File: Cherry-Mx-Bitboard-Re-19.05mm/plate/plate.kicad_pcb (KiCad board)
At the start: 2 copper layers, 106 x 106 mm, 396 parts, among them SW1 SW_Push

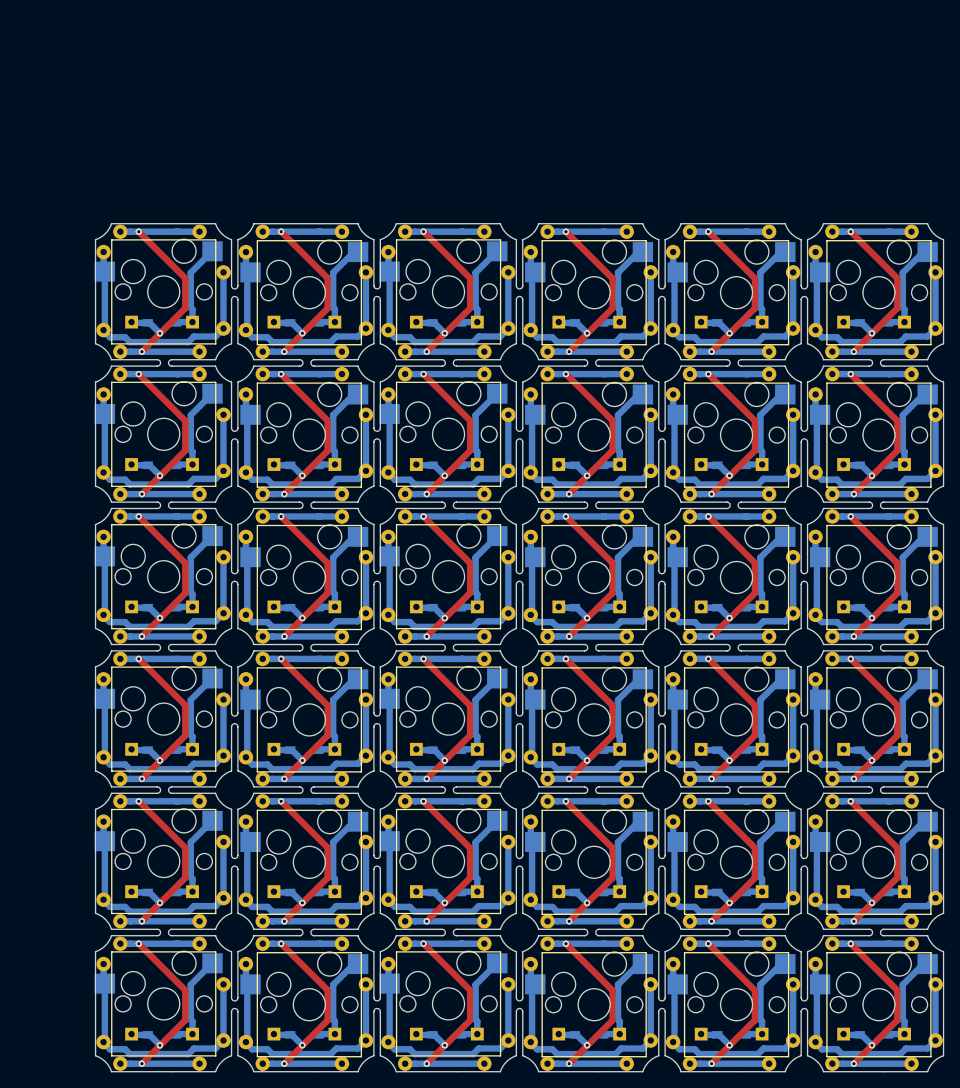
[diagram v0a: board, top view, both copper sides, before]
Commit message: Plate generaged with gerber
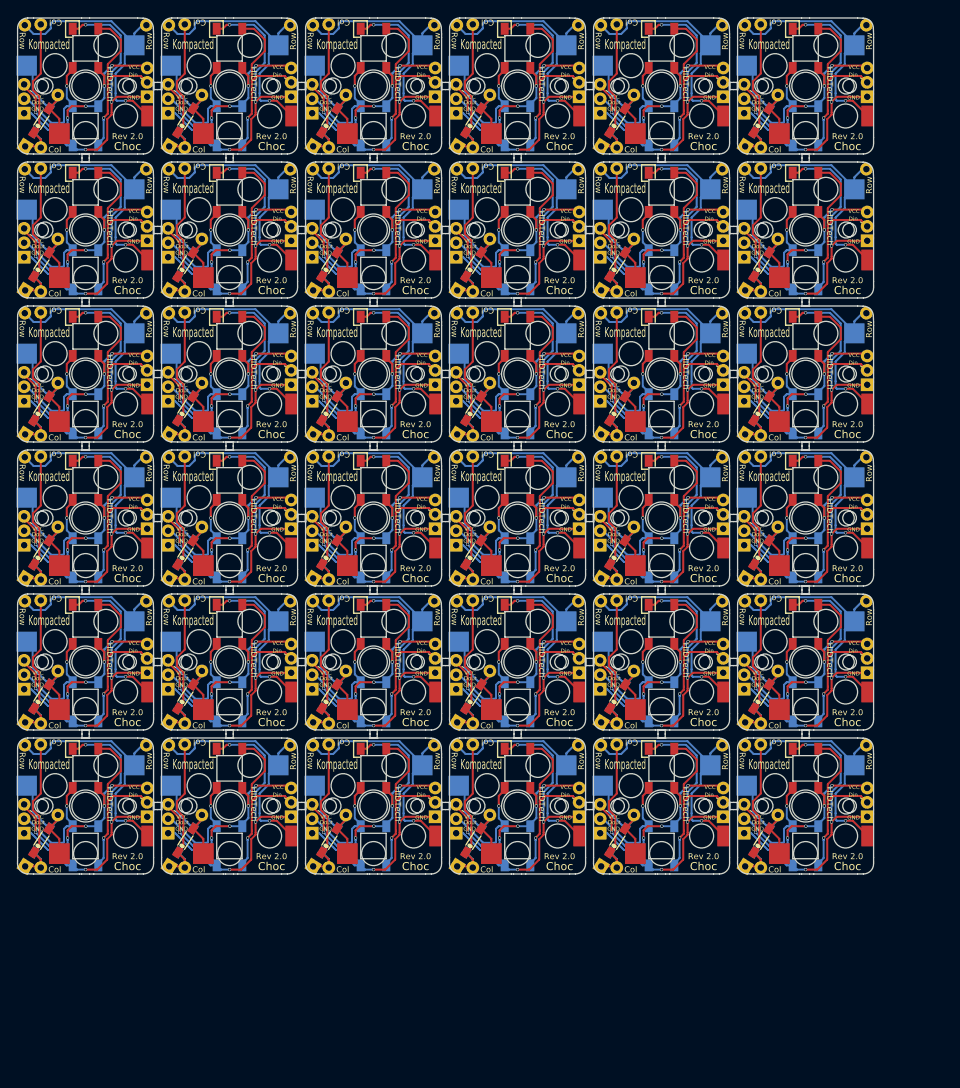
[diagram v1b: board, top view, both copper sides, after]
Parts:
- removed Col111 (x36), Col114 (x36), Row112 (x36), Row114 (x36): Conn_01x01, Footprints:Wirepad
- removed the Col112 at (178.1, 161.0)
- removed the Col112 at (124.7, 143.2)
- removed the Col112 at (142.5, 143.2)
- removed the Col112 at (106.9, 143.2)
- removed the Col112 at (178.1, 125.4)
- removed the Col112 at (195.9, 125.4)
- removed the Col112 at (160.3, 125.4)
- removed the Col112 at (124.7, 125.4)
- removed the Col112 at (142.5, 125.4)
- removed the Col112 at (106.9, 125.4)
- removed the Col112 at (178.1, 107.6)
- removed the Col112 at (195.9, 161.0)
- removed the Col112 at (195.9, 107.6)
- removed the Col112 at (160.3, 107.6)
- removed the Col112 at (124.7, 107.6)
- removed the Col112 at (142.5, 107.6)
- removed the Col112 at (106.9, 107.6)
- removed the Col112 at (195.9, 89.8)
- removed the Col112 at (178.1, 89.8)
- removed the Col112 at (124.7, 89.8)
- removed the Col112 at (160.3, 89.8)
- removed the Col112 at (142.5, 89.8)
- removed the Col112 at (160.3, 161.0)
- removed the Col112 at (106.9, 89.8)
- removed the Col112 at (195.9, 72.0)
- removed the Col112 at (178.1, 72.0)
- removed the Col112 at (160.3, 72.0)
- removed the Col112 at (142.5, 72.0)
- removed the Col112 at (124.7, 72.0)
- removed the Col112 at (106.9, 72.0)
- removed the Col112 at (124.7, 161.0)
- removed the Col112 at (142.5, 161.0)
- removed the Col112 at (106.9, 161.0)
- removed the Col112 at (178.1, 143.2)
- removed the Col112 at (195.9, 143.2)
- removed the Col112 at (160.3, 143.2)
- removed the Col113 at (186.0, 176.0)
- removed the Col113 at (114.8, 158.2)
- removed the Col113 at (168.2, 158.2)
- removed the Col113 at (97.0, 158.2)
- removed the Col113 at (186.0, 140.4)
- removed the Col113 at (150.4, 140.4)
- removed the Col113 at (132.6, 140.4)
- removed the Col113 at (114.8, 140.4)
- removed the Col113 at (168.2, 140.4)
- removed the Col113 at (97.0, 140.4)
- removed the Col113 at (186.0, 122.6)
- removed the Col113 at (150.4, 176.0)
- removed the Col113 at (150.4, 122.6)
- removed the Col113 at (132.6, 122.6)
- removed the Col113 at (114.8, 122.6)
- removed the Col113 at (168.2, 122.6)
- removed the Col113 at (97.0, 122.6)
- removed the Col113 at (186.0, 104.8)
- removed the Col113 at (168.2, 104.8)
- removed the Col113 at (114.8, 104.8)
- removed the Col113 at (132.6, 104.8)
- removed the Col113 at (150.4, 104.8)
- removed the Col113 at (132.6, 176.0)
- removed the Col113 at (97.0, 104.8)
- removed the Col113 at (186.0, 87.0)
- removed the Col113 at (168.2, 87.0)
- removed the Col113 at (150.4, 87.0)
- removed the Col113 at (132.6, 87.0)
- removed the Col113 at (114.8, 87.0)
- removed the Col113 at (97.0, 87.0)
- removed the Col113 at (114.8, 176.0)
- removed the Col113 at (168.2, 176.0)
- removed the Col113 at (97.0, 176.0)
- removed the Col113 at (186.0, 158.2)
- removed the Col113 at (150.4, 158.2)
- removed the Col113 at (132.6, 158.2)
- removed the D1 at (169.6, 172.3)
- removed the D1 at (134.0, 154.5)
- removed the D1 at (151.8, 154.5)
- removed the D1 at (98.4, 154.5)
- removed the D1 at (169.6, 136.7)
- removed the D1 at (187.4, 136.7)
- removed the D1 at (116.2, 136.7)
- removed the D1 at (134.0, 136.7)
- removed the D1 at (151.8, 136.7)
- removed the D1 at (98.4, 136.7)
- removed the D1 at (169.6, 118.9)
- removed the D1 at (187.4, 172.3)
- removed the D1 at (187.4, 118.9)
- removed the D1 at (116.2, 118.9)
- removed the D1 at (134.0, 118.9)
- removed the D1 at (151.8, 118.9)
- removed the D1 at (98.4, 118.9)
- removed the D1 at (187.4, 101.1)
- removed the D1 at (169.6, 101.1)
- removed the D1 at (116.2, 101.1)
- removed the D1 at (134.0, 101.1)
- removed the D1 at (151.8, 101.1)
- removed the D1 at (116.2, 172.3)
- removed the D1 at (98.4, 101.1)
- removed the D1 at (187.4, 83.3)
- removed the D1 at (169.6, 83.3)
- removed the D1 at (151.8, 83.3)
- removed the D1 at (134.0, 83.3)
- removed the D1 at (116.2, 83.3)
- removed the D1 at (98.4, 83.3)
- removed the D1 at (134.0, 172.3)
- removed the D1 at (151.8, 172.3)
- removed the D1 at (98.4, 172.3)
- removed the D1 at (169.6, 154.5)
- removed the D1 at (187.4, 154.5)
- removed the D1 at (116.2, 154.5)
- removed the D2 at (191.2, 172.4)
- removed the D2 at (155.6, 154.6)
- removed the D2 at (137.8, 154.6)
- removed the D2 at (102.2, 154.6)
- removed the D2 at (191.2, 136.8)
- removed the D2 at (120.0, 136.8)
- removed the D2 at (173.4, 136.8)
- removed the D2 at (155.6, 136.8)
- removed the D2 at (137.8, 136.8)
- removed the D2 at (102.2, 136.8)
- removed the D2 at (191.2, 119.0)
- removed the D2 at (120.0, 172.4)
- removed the D2 at (120.0, 119.0)
- removed the D2 at (173.4, 119.0)
- removed the D2 at (155.6, 119.0)
- removed the D2 at (137.8, 119.0)
- removed the D2 at (102.2, 119.0)
- removed the D2 at (191.2, 101.2)
- removed the D2 at (173.4, 101.2)
- removed the D2 at (120.0, 101.2)
- removed the D2 at (137.8, 101.2)
- removed the D2 at (155.6, 101.2)
- removed the D2 at (173.4, 172.4)
- removed the D2 at (102.2, 101.2)
- removed the D2 at (191.2, 83.4)
- removed the D2 at (173.4, 83.4)
- removed the D2 at (155.6, 83.4)
- removed the D2 at (137.8, 83.4)
- removed the D2 at (120.0, 83.4)
- removed the D2 at (102.2, 83.4)
- removed the D2 at (155.6, 172.4)
- removed the D2 at (137.8, 172.4)
- removed the D2 at (102.2, 172.4)
- removed the D2 at (191.2, 154.6)
- removed the D2 at (120.0, 154.6)
- removed the D2 at (173.4, 154.6)
- removed the Row111 at (183.9, 163.6)
- removed the Row111 at (112.7, 145.8)
- removed the Row111 at (94.9, 145.8)
- removed the Row111 at (148.3, 145.8)
- removed the Row111 at (183.9, 128.0)
- removed the Row111 at (166.1, 128.0)
- removed the Row111 at (130.5, 128.0)
- removed the Row111 at (112.7, 128.0)
- removed the Row111 at (94.9, 128.0)
- removed the Row111 at (148.3, 128.0)
- removed the Row111 at (183.9, 110.2)
- removed the Row111 at (166.1, 163.6)
- removed the Row111 at (166.1, 110.2)
- removed the Row111 at (130.5, 110.2)
- removed the Row111 at (112.7, 110.2)
- removed the Row111 at (94.9, 110.2)
- removed the Row111 at (148.3, 110.2)
- removed the Row111 at (183.9, 92.4)
- removed the Row111 at (166.1, 92.4)
- removed the Row111 at (112.7, 92.4)
- removed the Row111 at (130.5, 92.4)
- removed the Row111 at (148.3, 92.4)
- removed the Row111 at (130.5, 163.6)
- removed the Row111 at (94.9, 92.4)
- removed the Row111 at (183.9, 74.6)
- removed the Row111 at (166.1, 74.6)
- removed the Row111 at (148.3, 74.6)
- removed the Row111 at (130.5, 74.6)
- removed the Row111 at (112.7, 74.6)
- removed the Row111 at (112.7, 163.6)
- removed the Row111 at (94.9, 163.6)
- removed the Row111 at (148.3, 163.6)
- removed the Row111 at (183.9, 145.8)
- removed the Row111 at (166.1, 145.8)
- removed the Row111 at (130.5, 145.8)
- removed the Row113 at (181.1, 166.1)
- removed the Row113 at (163.3, 148.3)
- removed the Row113 at (127.7, 148.3)
- removed the Row113 at (145.5, 148.3)
- removed the Row113 at (181.1, 130.5)
- removed the Row113 at (198.9, 130.5)
- removed the Row113 at (109.9, 130.5)
- removed the Row113 at (163.3, 130.5)
- removed the Row113 at (127.7, 130.5)
- removed the Row113 at (145.5, 130.5)
- removed the Row113 at (181.1, 112.7)
- removed the Row113 at (198.9, 166.1)
- removed the Row113 at (198.9, 112.7)
- removed the Row113 at (109.9, 112.7)
- removed the Row113 at (163.3, 112.7)
- removed the Row113 at (127.7, 112.7)
- removed the Row113 at (145.5, 112.7)
- removed the Row113 at (198.9, 94.9)
- removed the Row113 at (181.1, 94.9)
- removed the Row113 at (109.9, 94.9)
- removed the Row113 at (127.7, 94.9)
- removed the Row113 at (163.3, 94.9)
- removed the Row113 at (109.9, 166.1)
- removed the Row113 at (145.5, 94.9)
- removed the Row113 at (198.9, 77.1)
- removed the Row113 at (181.1, 77.1)
- removed the Row113 at (145.5, 77.1)
- removed the Row113 at (163.3, 77.1)
- removed the Row113 at (127.7, 77.1)
- removed the Row113 at (163.3, 166.1)
- removed the Row113 at (127.7, 166.1)
- removed the Row113 at (145.5, 166.1)
- removed the Row113 at (181.1, 148.3)
- removed the Row113 at (198.9, 148.3)
- removed the Row113 at (109.9, 148.3)
- removed the SW1 at (191.8, 168.7)
- removed the SW1 at (138.0, 150.8)
- removed the SW1 at (156.2, 150.9)
- removed the SW1 at (102.4, 150.8)
- removed the SW1 at (191.8, 133.1)
- removed the SW1 at (174.0, 133.1)
- removed the SW1 at (120.6, 133.1)
- removed the SW1 at (138.0, 133.0)
- removed the SW1 at (156.2, 133.1)
- removed the SW1 at (102.4, 133.0)
- removed the SW1 at (191.8, 115.3)
- removed the SW1 at (174.0, 168.7)
- removed the SW1 at (174.0, 115.3)
- removed the SW1 at (120.6, 115.3)
- removed the SW1 at (138.0, 115.2)
- removed the SW1 at (156.2, 115.3)
- removed the SW1 at (102.4, 115.2)
- removed the SW1 at (191.8, 97.5)
- removed the SW1 at (174.0, 97.5)
- removed the SW1 at (120.6, 97.5)
- removed the SW1 at (156.2, 97.5)
- removed the SW1 at (138.0, 97.4)
- removed the SW1 at (120.6, 168.7)
- removed the SW1 at (102.4, 97.4)
- removed the SW1 at (191.8, 79.7)
- removed the SW1 at (174.0, 79.7)
- removed the SW1 at (156.2, 79.7)
- removed the SW1 at (138.0, 79.6)
- removed the SW1 at (120.6, 79.7)
- removed the SW1 at (102.4, 79.6)
- removed the SW1 at (138.0, 168.6)
- removed the SW1 at (156.2, 168.7)
- removed the SW1 at (102.4, 168.6)
- removed the SW1 at (191.8, 150.9)
- removed the SW1 at (174.0, 150.9)
- removed the SW1 at (120.6, 150.9)
- added Col112: Conn_01x01, Footprints:Wirepad, F.Cu at (87.0, 118.1)
- added Col112: Conn_01x01, Footprints:Wirepad, F.Cu at (177.0, 118.1)
- added Col112: Conn_01x01, Footprints:Wirepad, F.Cu at (141.0, 118.1)
- added Col112: Conn_01x01, Footprints:Wirepad, F.Cu at (123.0, 118.1)
- added Col112: Conn_01x01, Footprints:Wirepad, F.Cu at (87.0, 82.1)
- added Col112: Conn_01x01, Footprints:Wirepad, F.Cu at (105.0, 82.1)
- added Col112: Conn_01x01, Footprints:Wirepad, F.Cu at (87.0, 100.1)
- added Col112: Conn_01x01, Footprints:Wirepad, F.Cu at (105.0, 100.1)
- added Col112: Conn_01x01, Footprints:Wirepad, F.Cu at (159.0, 100.1)
- added Col112: Conn_01x01, Footprints:Wirepad, F.Cu at (177.0, 100.1)
- added Col112: Conn_01x01, Footprints:Wirepad, F.Cu at (123.0, 100.1)
- added Col112: Conn_01x01, Footprints:Wirepad, F.Cu at (105.0, 118.1)
- added Col112: Conn_01x01, Footprints:Wirepad, F.Cu at (141.0, 100.1)
- added Col112: Conn_01x01, Footprints:Wirepad, F.Cu at (159.0, 82.1)
- added Col112: Conn_01x01, Footprints:Wirepad, F.Cu at (177.0, 82.1)
- added Col112: Conn_01x01, Footprints:Wirepad, F.Cu at (141.0, 82.1)
- added Col112: Conn_01x01, Footprints:Wirepad, F.Cu at (123.0, 82.1)
- added Col112: Conn_01x01, Footprints:Wirepad, F.Cu at (87.0, 64.1)
- added Col112: Conn_01x01, Footprints:Wirepad, F.Cu at (105.0, 64.1)
- added Col112: Conn_01x01, Footprints:Wirepad, F.Cu at (159.0, 64.1)
- added Col112: Conn_01x01, Footprints:Wirepad, F.Cu at (177.0, 64.1)
- added Col112: Conn_01x01, Footprints:Wirepad, F.Cu at (141.0, 64.1)
- added Col112: Conn_01x01, Footprints:Wirepad, F.Cu at (87.0, 136.1)
- added Col112: Conn_01x01, Footprints:Wirepad, F.Cu at (123.0, 64.1)
- added Col112: Conn_01x01, Footprints:Wirepad, F.Cu at (159.0, 46.1)
- added Col112: Conn_01x01, Footprints:Wirepad, F.Cu at (177.0, 46.1)
- added Col112: Conn_01x01, Footprints:Wirepad, F.Cu at (123.0, 46.1)
- added Col112: Conn_01x01, Footprints:Wirepad, F.Cu at (141.0, 46.1)
- added Col112: Conn_01x01, Footprints:Wirepad, F.Cu at (105.0, 46.1)
- added Col112: Conn_01x01, Footprints:Wirepad, F.Cu at (87.0, 46.1)
- added Col112: Conn_01x01, Footprints:Wirepad, F.Cu at (105.0, 136.1)
- added Col112: Conn_01x01, Footprints:Wirepad, F.Cu at (159.0, 136.1)
- added Col112: Conn_01x01, Footprints:Wirepad, F.Cu at (177.0, 136.1)
- added Col112: Conn_01x01, Footprints:Wirepad, F.Cu at (123.0, 136.1)
- added Col112: Conn_01x01, Footprints:Wirepad, F.Cu at (141.0, 136.1)
- added Col112: Conn_01x01, Footprints:Wirepad, F.Cu at (159.0, 118.1)
- added Col113: Conn_01x01, Footprints:Wirepad, F.Cu at (87.0, 133.5)
- added Col113: Conn_01x01, Footprints:Wirepad, F.Cu at (177.0, 133.5)
- added Col113: Conn_01x01, Footprints:Wirepad, F.Cu at (141.0, 133.5)
- added Col113: Conn_01x01, Footprints:Wirepad, F.Cu at (123.0, 133.5)
- added Col113: Conn_01x01, Footprints:Wirepad, F.Cu at (87.0, 97.5)
- added Col113: Conn_01x01, Footprints:Wirepad, F.Cu at (105.0, 97.5)
- added Col113: Conn_01x01, Footprints:Wirepad, F.Cu at (87.0, 115.5)
- added Col113: Conn_01x01, Footprints:Wirepad, F.Cu at (105.0, 115.5)
- added Col113: Conn_01x01, Footprints:Wirepad, F.Cu at (159.0, 115.5)
- added Col113: Conn_01x01, Footprints:Wirepad, F.Cu at (177.0, 115.5)
- added Col113: Conn_01x01, Footprints:Wirepad, F.Cu at (123.0, 115.5)
- added Col113: Conn_01x01, Footprints:Wirepad, F.Cu at (105.0, 133.5)
- added Col113: Conn_01x01, Footprints:Wirepad, F.Cu at (141.0, 115.5)
- added Col113: Conn_01x01, Footprints:Wirepad, F.Cu at (159.0, 97.5)
- added Col113: Conn_01x01, Footprints:Wirepad, F.Cu at (177.0, 97.5)
- added Col113: Conn_01x01, Footprints:Wirepad, F.Cu at (141.0, 97.5)
- added Col113: Conn_01x01, Footprints:Wirepad, F.Cu at (123.0, 97.5)
- added Col113: Conn_01x01, Footprints:Wirepad, F.Cu at (87.0, 79.5)
- added Col113: Conn_01x01, Footprints:Wirepad, F.Cu at (105.0, 79.5)
- added Col113: Conn_01x01, Footprints:Wirepad, F.Cu at (159.0, 79.5)
- added Col113: Conn_01x01, Footprints:Wirepad, F.Cu at (177.0, 79.5)
- added Col113: Conn_01x01, Footprints:Wirepad, F.Cu at (141.0, 79.5)
- added Col113: Conn_01x01, Footprints:Wirepad, F.Cu at (87.0, 151.5)
- added Col113: Conn_01x01, Footprints:Wirepad, F.Cu at (123.0, 79.5)
- added Col113: Conn_01x01, Footprints:Wirepad, F.Cu at (159.0, 61.5)
- added Col113: Conn_01x01, Footprints:Wirepad, F.Cu at (177.0, 61.5)
- added Col113: Conn_01x01, Footprints:Wirepad, F.Cu at (123.0, 61.5)
- added Col113: Conn_01x01, Footprints:Wirepad, F.Cu at (141.0, 61.5)
- added Col113: Conn_01x01, Footprints:Wirepad, F.Cu at (105.0, 61.5)
- added Col113: Conn_01x01, Footprints:Wirepad, F.Cu at (87.0, 61.5)
- added Col113: Conn_01x01, Footprints:Wirepad, F.Cu at (105.0, 151.5)
- added Col113: Conn_01x01, Footprints:Wirepad, F.Cu at (159.0, 151.5)
- added Col113: Conn_01x01, Footprints:Wirepad, F.Cu at (177.0, 151.5)
- added Col113: Conn_01x01, Footprints:Wirepad, F.Cu at (123.0, 151.5)
- added Col113: Conn_01x01, Footprints:Wirepad, F.Cu at (141.0, 151.5)
- added Col113: Conn_01x01, Footprints:Wirepad, F.Cu at (159.0, 133.5)
- added D1: 1N4148W, Footprints:1N4148W, B.Cu at (85.1, 133.4)
- added D1: 1N4148W, Footprints:1N4148W, B.Cu at (157.1, 133.4)
- added D1: 1N4148W, Footprints:1N4148W, B.Cu at (121.1, 133.4)
- added D1: 1N4148W, Footprints:1N4148W, B.Cu at (139.1, 133.4)
- added D1: 1N4148W, Footprints:1N4148W, B.Cu at (85.1, 97.4)
- added D1: 1N4148W, Footprints:1N4148W, B.Cu at (103.1, 97.4)
- added D1: 1N4148W, Footprints:1N4148W, B.Cu at (85.1, 115.4)
- added D1: 1N4148W, Footprints:1N4148W, B.Cu at (103.1, 115.4)
- added D1: 1N4148W, Footprints:1N4148W, B.Cu at (175.1, 115.4)
- added D1: 1N4148W, Footprints:1N4148W, B.Cu at (157.1, 115.4)
- added D1: 1N4148W, Footprints:1N4148W, B.Cu at (121.1, 115.4)
- added D1: 1N4148W, Footprints:1N4148W, B.Cu at (103.1, 133.4)
- added D1: 1N4148W, Footprints:1N4148W, B.Cu at (139.1, 115.4)
- added D1: 1N4148W, Footprints:1N4148W, B.Cu at (175.1, 97.4)
- added D1: 1N4148W, Footprints:1N4148W, B.Cu at (157.1, 97.4)
- added D1: 1N4148W, Footprints:1N4148W, B.Cu at (121.1, 97.4)
- added D1: 1N4148W, Footprints:1N4148W, B.Cu at (139.1, 97.4)
- added D1: 1N4148W, Footprints:1N4148W, B.Cu at (85.1, 79.4)
- added D1: 1N4148W, Footprints:1N4148W, B.Cu at (103.1, 79.4)
- added D1: 1N4148W, Footprints:1N4148W, B.Cu at (175.1, 79.4)
- added D1: 1N4148W, Footprints:1N4148W, B.Cu at (157.1, 79.4)
- added D1: 1N4148W, Footprints:1N4148W, B.Cu at (121.1, 79.4)
- added D1: 1N4148W, Footprints:1N4148W, B.Cu at (85.1, 151.4)
- added D1: 1N4148W, Footprints:1N4148W, B.Cu at (139.1, 79.4)
- added D1: 1N4148W, Footprints:1N4148W, B.Cu at (157.1, 61.4)
- added D1: 1N4148W, Footprints:1N4148W, B.Cu at (175.1, 61.4)
- added D1: 1N4148W, Footprints:1N4148W, B.Cu at (121.1, 61.4)
- added D1: 1N4148W, Footprints:1N4148W, B.Cu at (139.1, 61.4)
- added D1: 1N4148W, Footprints:1N4148W, B.Cu at (103.1, 61.4)
- added D1: 1N4148W, Footprints:1N4148W, B.Cu at (85.1, 61.4)
- added D1: 1N4148W, Footprints:1N4148W, B.Cu at (103.1, 151.4)
- added D1: 1N4148W, Footprints:1N4148W, B.Cu at (175.1, 151.4)
- added D1: 1N4148W, Footprints:1N4148W, B.Cu at (157.1, 151.4)
- added D1: 1N4148W, Footprints:1N4148W, B.Cu at (121.1, 151.4)
- added D1: 1N4148W, Footprints:1N4148W, B.Cu at (139.1, 151.4)
- added D1: 1N4148W, Footprints:1N4148W, B.Cu at (175.1, 133.4)
- added D2: 1N4148W, Footprints:1N4148W, B.Cu at (87.1, 130.1)
- added D2: 1N4148W, Footprints:1N4148W, B.Cu at (177.1, 130.1)
- added D2: 1N4148W, Footprints:1N4148W, B.Cu at (141.1, 130.1)
- added D2: 1N4148W, Footprints:1N4148W, B.Cu at (123.1, 130.1)
- added D2: 1N4148W, Footprints:1N4148W, B.Cu at (87.1, 94.1)
- added D2: 1N4148W, Footprints:1N4148W, B.Cu at (105.1, 94.1)
- added D2: 1N4148W, Footprints:1N4148W, B.Cu at (87.1, 112.1)
- added D2: 1N4148W, Footprints:1N4148W, B.Cu at (105.1, 112.1)
- added D2: 1N4148W, Footprints:1N4148W, B.Cu at (159.1, 112.1)
- added D2: 1N4148W, Footprints:1N4148W, B.Cu at (177.1, 112.1)
- added D2: 1N4148W, Footprints:1N4148W, B.Cu at (141.1, 112.1)
- added D2: 1N4148W, Footprints:1N4148W, B.Cu at (105.1, 130.1)
- added D2: 1N4148W, Footprints:1N4148W, B.Cu at (123.1, 112.1)
- added D2: 1N4148W, Footprints:1N4148W, B.Cu at (159.1, 94.1)
- added D2: 1N4148W, Footprints:1N4148W, B.Cu at (177.1, 94.1)
- added D2: 1N4148W, Footprints:1N4148W, B.Cu at (141.1, 94.1)
- added D2: 1N4148W, Footprints:1N4148W, B.Cu at (123.1, 94.1)
- added D2: 1N4148W, Footprints:1N4148W, B.Cu at (87.1, 76.1)
- added D2: 1N4148W, Footprints:1N4148W, B.Cu at (105.1, 76.1)
- added D2: 1N4148W, Footprints:1N4148W, B.Cu at (159.1, 76.1)
- added D2: 1N4148W, Footprints:1N4148W, B.Cu at (177.1, 76.1)
- added D2: 1N4148W, Footprints:1N4148W, B.Cu at (141.1, 76.1)
- added D2: 1N4148W, Footprints:1N4148W, B.Cu at (87.1, 148.1)
- added D2: 1N4148W, Footprints:1N4148W, B.Cu at (123.1, 76.1)
- added D2: 1N4148W, Footprints:1N4148W, B.Cu at (159.1, 58.1)
- added D2: 1N4148W, Footprints:1N4148W, B.Cu at (177.1, 58.1)
- added D2: 1N4148W, Footprints:1N4148W, B.Cu at (123.1, 58.1)
- added D2: 1N4148W, Footprints:1N4148W, B.Cu at (141.1, 58.1)
- added D2: 1N4148W, Footprints:1N4148W, B.Cu at (105.1, 58.1)
- added D2: 1N4148W, Footprints:1N4148W, B.Cu at (87.1, 58.1)
- added D2: 1N4148W, Footprints:1N4148W, B.Cu at (105.1, 148.1)
- added D2: 1N4148W, Footprints:1N4148W, B.Cu at (159.1, 148.1)
- added D2: 1N4148W, Footprints:1N4148W, B.Cu at (177.1, 148.1)
- added D2: 1N4148W, Footprints:1N4148W, B.Cu at (141.1, 148.1)
- added D2: 1N4148W, Footprints:1N4148W, B.Cu at (123.1, 148.1)
- added D2: 1N4148W, Footprints:1N4148W, B.Cu at (159.1, 130.1)
- added D3: 1N4148W, Footprints:1N4148W, F.Cu at (87.1, 130.1)
- added D3: 1N4148W, Footprints:1N4148W, F.Cu at (177.1, 130.1)
- added D3: 1N4148W, Footprints:1N4148W, F.Cu at (141.1, 130.1)
- added D3: 1N4148W, Footprints:1N4148W, F.Cu at (123.1, 130.1)
- added D3: 1N4148W, Footprints:1N4148W, F.Cu at (87.1, 94.1)
- added D3: 1N4148W, Footprints:1N4148W, F.Cu at (105.1, 94.1)
- added D3: 1N4148W, Footprints:1N4148W, F.Cu at (87.1, 112.1)
- added D3: 1N4148W, Footprints:1N4148W, F.Cu at (105.1, 112.1)
- added D3: 1N4148W, Footprints:1N4148W, F.Cu at (159.1, 112.1)
- added D3: 1N4148W, Footprints:1N4148W, F.Cu at (177.1, 112.1)
- added D3: 1N4148W, Footprints:1N4148W, F.Cu at (123.1, 112.1)
- added D3: 1N4148W, Footprints:1N4148W, F.Cu at (105.1, 130.1)
- added D3: 1N4148W, Footprints:1N4148W, F.Cu at (141.1, 112.1)
- added D3: 1N4148W, Footprints:1N4148W, F.Cu at (159.1, 94.1)
- added D3: 1N4148W, Footprints:1N4148W, F.Cu at (177.1, 94.1)
- added D3: 1N4148W, Footprints:1N4148W, F.Cu at (141.1, 94.1)
- added D3: 1N4148W, Footprints:1N4148W, F.Cu at (123.1, 94.1)
- added D3: 1N4148W, Footprints:1N4148W, F.Cu at (87.1, 76.1)
- added D3: 1N4148W, Footprints:1N4148W, F.Cu at (105.1, 76.1)
- added D3: 1N4148W, Footprints:1N4148W, F.Cu at (159.1, 76.1)
- added D3: 1N4148W, Footprints:1N4148W, F.Cu at (177.1, 76.1)
- added D3: 1N4148W, Footprints:1N4148W, F.Cu at (141.1, 76.1)
- added D3: 1N4148W, Footprints:1N4148W, F.Cu at (87.1, 148.1)
- added D3: 1N4148W, Footprints:1N4148W, F.Cu at (123.1, 76.1)
- added D3: 1N4148W, Footprints:1N4148W, F.Cu at (159.1, 58.1)
- added D3: 1N4148W, Footprints:1N4148W, F.Cu at (177.1, 58.1)
- added D3: 1N4148W, Footprints:1N4148W, F.Cu at (123.1, 58.1)
- added D3: 1N4148W, Footprints:1N4148W, F.Cu at (141.1, 58.1)
- added D3: 1N4148W, Footprints:1N4148W, F.Cu at (105.1, 58.1)
- added D3: 1N4148W, Footprints:1N4148W, F.Cu at (87.1, 58.1)
- added D3: 1N4148W, Footprints:1N4148W, F.Cu at (105.1, 148.1)
- added D3: 1N4148W, Footprints:1N4148W, F.Cu at (159.1, 148.1)
- added D3: 1N4148W, Footprints:1N4148W, F.Cu at (177.1, 148.1)
- added D3: 1N4148W, Footprints:1N4148W, F.Cu at (123.1, 148.1)
- added D3: 1N4148W, Footprints:1N4148W, F.Cu at (141.1, 148.1)
- added D3: 1N4148W, Footprints:1N4148W, F.Cu at (159.1, 130.1)
- added D5: SK6812, customs:LED_SK6812_PLCC4_5.0x5.0mm_P3.2mm_FLIP, B.Cu at (92.6, 130.8)
- added D5: SK6812, customs:LED_SK6812_PLCC4_5.0x5.0mm_P3.2mm_FLIP, B.Cu at (164.6, 130.8)
- added D5: SK6812, customs:LED_SK6812_PLCC4_5.0x5.0mm_P3.2mm_FLIP, B.Cu at (128.6, 130.8)
- added D5: SK6812, customs:LED_SK6812_PLCC4_5.0x5.0mm_P3.2mm_FLIP, B.Cu at (146.6, 130.8)
- added D5: SK6812, customs:LED_SK6812_PLCC4_5.0x5.0mm_P3.2mm_FLIP, B.Cu at (92.6, 94.8)
- added D5: SK6812, customs:LED_SK6812_PLCC4_5.0x5.0mm_P3.2mm_FLIP, B.Cu at (110.6, 94.8)
- added D5: SK6812, customs:LED_SK6812_PLCC4_5.0x5.0mm_P3.2mm_FLIP, B.Cu at (92.6, 112.8)
- added D5: SK6812, customs:LED_SK6812_PLCC4_5.0x5.0mm_P3.2mm_FLIP, B.Cu at (110.6, 112.8)
- added D5: SK6812, customs:LED_SK6812_PLCC4_5.0x5.0mm_P3.2mm_FLIP, B.Cu at (182.6, 112.8)
- added D5: SK6812, customs:LED_SK6812_PLCC4_5.0x5.0mm_P3.2mm_FLIP, B.Cu at (164.6, 112.8)
- added D5: SK6812, customs:LED_SK6812_PLCC4_5.0x5.0mm_P3.2mm_FLIP, B.Cu at (128.6, 112.8)
- added D5: SK6812, customs:LED_SK6812_PLCC4_5.0x5.0mm_P3.2mm_FLIP, B.Cu at (110.6, 130.8)
- added D5: SK6812, customs:LED_SK6812_PLCC4_5.0x5.0mm_P3.2mm_FLIP, B.Cu at (146.6, 112.8)
- added D5: SK6812, customs:LED_SK6812_PLCC4_5.0x5.0mm_P3.2mm_FLIP, B.Cu at (182.6, 94.8)
- added D5: SK6812, customs:LED_SK6812_PLCC4_5.0x5.0mm_P3.2mm_FLIP, B.Cu at (164.6, 94.8)
- added D5: SK6812, customs:LED_SK6812_PLCC4_5.0x5.0mm_P3.2mm_FLIP, B.Cu at (128.6, 94.8)
- added D5: SK6812, customs:LED_SK6812_PLCC4_5.0x5.0mm_P3.2mm_FLIP, B.Cu at (146.6, 94.8)
- added D5: SK6812, customs:LED_SK6812_PLCC4_5.0x5.0mm_P3.2mm_FLIP, B.Cu at (92.6, 76.8)
- added D5: SK6812, customs:LED_SK6812_PLCC4_5.0x5.0mm_P3.2mm_FLIP, B.Cu at (110.6, 76.8)
- added D5: SK6812, customs:LED_SK6812_PLCC4_5.0x5.0mm_P3.2mm_FLIP, B.Cu at (182.6, 76.8)
- added D5: SK6812, customs:LED_SK6812_PLCC4_5.0x5.0mm_P3.2mm_FLIP, B.Cu at (164.6, 76.8)
- added D5: SK6812, customs:LED_SK6812_PLCC4_5.0x5.0mm_P3.2mm_FLIP, B.Cu at (128.6, 76.8)
- added D5: SK6812, customs:LED_SK6812_PLCC4_5.0x5.0mm_P3.2mm_FLIP, B.Cu at (92.6, 148.8)
- added D5: SK6812, customs:LED_SK6812_PLCC4_5.0x5.0mm_P3.2mm_FLIP, B.Cu at (146.6, 76.8)
- added D5: SK6812, customs:LED_SK6812_PLCC4_5.0x5.0mm_P3.2mm_FLIP, B.Cu at (164.6, 58.8)
- added D5: SK6812, customs:LED_SK6812_PLCC4_5.0x5.0mm_P3.2mm_FLIP, B.Cu at (182.6, 58.8)
- added D5: SK6812, customs:LED_SK6812_PLCC4_5.0x5.0mm_P3.2mm_FLIP, B.Cu at (128.6, 58.8)
- added D5: SK6812, customs:LED_SK6812_PLCC4_5.0x5.0mm_P3.2mm_FLIP, B.Cu at (146.6, 58.8)
- added D5: SK6812, customs:LED_SK6812_PLCC4_5.0x5.0mm_P3.2mm_FLIP, B.Cu at (110.6, 58.8)
- added D5: SK6812, customs:LED_SK6812_PLCC4_5.0x5.0mm_P3.2mm_FLIP, B.Cu at (92.6, 58.8)
- added D5: SK6812, customs:LED_SK6812_PLCC4_5.0x5.0mm_P3.2mm_FLIP, B.Cu at (110.6, 148.8)
- added D5: SK6812, customs:LED_SK6812_PLCC4_5.0x5.0mm_P3.2mm_FLIP, B.Cu at (182.6, 148.8)
- added D5: SK6812, customs:LED_SK6812_PLCC4_5.0x5.0mm_P3.2mm_FLIP, B.Cu at (164.6, 148.8)
- added D5: SK6812, customs:LED_SK6812_PLCC4_5.0x5.0mm_P3.2mm_FLIP, B.Cu at (128.6, 148.8)
- added D5: SK6812, customs:LED_SK6812_PLCC4_5.0x5.0mm_P3.2mm_FLIP, B.Cu at (146.6, 148.8)
- added D5: SK6812, customs:LED_SK6812_PLCC4_5.0x5.0mm_P3.2mm_FLIP, B.Cu at (182.6, 130.8)
- added D6: SK6812, customs:LED_SK6812_PLCC4_5.0x5.0mm_P3.2mm_FLIP, F.Cu at (92.6, 121.1)
- added D6: SK6812, customs:LED_SK6812_PLCC4_5.0x5.0mm_P3.2mm_FLIP, F.Cu at (164.6, 121.1)
- added D6: SK6812, customs:LED_SK6812_PLCC4_5.0x5.0mm_P3.2mm_FLIP, F.Cu at (146.6, 121.1)
- added D6: SK6812, customs:LED_SK6812_PLCC4_5.0x5.0mm_P3.2mm_FLIP, F.Cu at (128.6, 121.1)
- added D6: SK6812, customs:LED_SK6812_PLCC4_5.0x5.0mm_P3.2mm_FLIP, F.Cu at (92.6, 85.1)
- added D6: SK6812, customs:LED_SK6812_PLCC4_5.0x5.0mm_P3.2mm_FLIP, F.Cu at (110.6, 85.1)
- added D6: SK6812, customs:LED_SK6812_PLCC4_5.0x5.0mm_P3.2mm_FLIP, F.Cu at (92.6, 103.1)
- added D6: SK6812, customs:LED_SK6812_PLCC4_5.0x5.0mm_P3.2mm_FLIP, F.Cu at (110.6, 103.1)
- added D6: SK6812, customs:LED_SK6812_PLCC4_5.0x5.0mm_P3.2mm_FLIP, F.Cu at (182.6, 103.1)
- added D6: SK6812, customs:LED_SK6812_PLCC4_5.0x5.0mm_P3.2mm_FLIP, F.Cu at (164.6, 103.1)
- added D6: SK6812, customs:LED_SK6812_PLCC4_5.0x5.0mm_P3.2mm_FLIP, F.Cu at (146.6, 103.1)
- added D6: SK6812, customs:LED_SK6812_PLCC4_5.0x5.0mm_P3.2mm_FLIP, F.Cu at (110.6, 121.1)
- added D6: SK6812, customs:LED_SK6812_PLCC4_5.0x5.0mm_P3.2mm_FLIP, F.Cu at (128.6, 103.1)
- added D6: SK6812, customs:LED_SK6812_PLCC4_5.0x5.0mm_P3.2mm_FLIP, F.Cu at (182.6, 85.1)
- added D6: SK6812, customs:LED_SK6812_PLCC4_5.0x5.0mm_P3.2mm_FLIP, F.Cu at (164.6, 85.1)
- added D6: SK6812, customs:LED_SK6812_PLCC4_5.0x5.0mm_P3.2mm_FLIP, F.Cu at (146.6, 85.1)
- added D6: SK6812, customs:LED_SK6812_PLCC4_5.0x5.0mm_P3.2mm_FLIP, F.Cu at (128.6, 85.1)
- added D6: SK6812, customs:LED_SK6812_PLCC4_5.0x5.0mm_P3.2mm_FLIP, F.Cu at (92.6, 67.1)
- added D6: SK6812, customs:LED_SK6812_PLCC4_5.0x5.0mm_P3.2mm_FLIP, F.Cu at (110.6, 67.1)
- added D6: SK6812, customs:LED_SK6812_PLCC4_5.0x5.0mm_P3.2mm_FLIP, F.Cu at (182.6, 67.1)
- added D6: SK6812, customs:LED_SK6812_PLCC4_5.0x5.0mm_P3.2mm_FLIP, F.Cu at (164.6, 67.1)
- added D6: SK6812, customs:LED_SK6812_PLCC4_5.0x5.0mm_P3.2mm_FLIP, F.Cu at (146.6, 67.1)
- added D6: SK6812, customs:LED_SK6812_PLCC4_5.0x5.0mm_P3.2mm_FLIP, F.Cu at (92.6, 139.1)
- added D6: SK6812, customs:LED_SK6812_PLCC4_5.0x5.0mm_P3.2mm_FLIP, F.Cu at (128.6, 67.1)
- added D6: SK6812, customs:LED_SK6812_PLCC4_5.0x5.0mm_P3.2mm_FLIP, F.Cu at (164.6, 49.1)
- added D6: SK6812, customs:LED_SK6812_PLCC4_5.0x5.0mm_P3.2mm_FLIP, F.Cu at (182.6, 49.1)
- added D6: SK6812, customs:LED_SK6812_PLCC4_5.0x5.0mm_P3.2mm_FLIP, F.Cu at (128.6, 49.1)
- added D6: SK6812, customs:LED_SK6812_PLCC4_5.0x5.0mm_P3.2mm_FLIP, F.Cu at (146.6, 49.1)
- added D6: SK6812, customs:LED_SK6812_PLCC4_5.0x5.0mm_P3.2mm_FLIP, F.Cu at (110.6, 49.1)
- added D6: SK6812, customs:LED_SK6812_PLCC4_5.0x5.0mm_P3.2mm_FLIP, F.Cu at (92.6, 49.1)
- added D6: SK6812, customs:LED_SK6812_PLCC4_5.0x5.0mm_P3.2mm_FLIP, F.Cu at (110.6, 139.1)
- added D6: SK6812, customs:LED_SK6812_PLCC4_5.0x5.0mm_P3.2mm_FLIP, F.Cu at (182.6, 139.1)
- added D6: SK6812, customs:LED_SK6812_PLCC4_5.0x5.0mm_P3.2mm_FLIP, F.Cu at (164.6, 139.1)
- added D6: SK6812, customs:LED_SK6812_PLCC4_5.0x5.0mm_P3.2mm_FLIP, F.Cu at (146.6, 139.1)
- added D6: SK6812, customs:LED_SK6812_PLCC4_5.0x5.0mm_P3.2mm_FLIP, F.Cu at (128.6, 139.1)
- added D6: SK6812, customs:LED_SK6812_PLCC4_5.0x5.0mm_P3.2mm_FLIP, F.Cu at (182.6, 121.1)
- added Din1: Conn_01x01, Footprints:Wirepad, F.Cu at (100.3, 125.4)
- added Din1: Conn_01x01, Footprints:Wirepad, F.Cu at (172.3, 125.4)
- added Din1: Conn_01x01, Footprints:Wirepad, F.Cu at (154.3, 125.4)
- added Din1: Conn_01x01, Footprints:Wirepad, F.Cu at (136.3, 125.4)
- added Din1: Conn_01x01, Footprints:Wirepad, F.Cu at (100.3, 89.4)
- added Din1: Conn_01x01, Footprints:Wirepad, F.Cu at (118.3, 89.4)
- added Din1: Conn_01x01, Footprints:Wirepad, F.Cu at (100.3, 107.4)
- added Din1: Conn_01x01, Footprints:Wirepad, F.Cu at (118.3, 107.4)
- added Din1: Conn_01x01, Footprints:Wirepad, F.Cu at (190.3, 107.4)
- added Din1: Conn_01x01, Footprints:Wirepad, F.Cu at (172.3, 107.4)
- added Din1: Conn_01x01, Footprints:Wirepad, F.Cu at (154.3, 107.4)
- added Din1: Conn_01x01, Footprints:Wirepad, F.Cu at (118.3, 125.4)
- added Din1: Conn_01x01, Footprints:Wirepad, F.Cu at (136.3, 107.4)
- added Din1: Conn_01x01, Footprints:Wirepad, F.Cu at (190.3, 89.4)
- added Din1: Conn_01x01, Footprints:Wirepad, F.Cu at (172.3, 89.4)
- added Din1: Conn_01x01, Footprints:Wirepad, F.Cu at (154.3, 89.4)
- added Din1: Conn_01x01, Footprints:Wirepad, F.Cu at (136.3, 89.4)
- added Din1: Conn_01x01, Footprints:Wirepad, F.Cu at (100.3, 71.4)
- added Din1: Conn_01x01, Footprints:Wirepad, F.Cu at (118.3, 71.4)
- added Din1: Conn_01x01, Footprints:Wirepad, F.Cu at (190.3, 71.4)
- added Din1: Conn_01x01, Footprints:Wirepad, F.Cu at (172.3, 71.4)
- added Din1: Conn_01x01, Footprints:Wirepad, F.Cu at (154.3, 71.4)
- added Din1: Conn_01x01, Footprints:Wirepad, F.Cu at (100.3, 143.4)
- added Din1: Conn_01x01, Footprints:Wirepad, F.Cu at (136.3, 71.4)
- added Din1: Conn_01x01, Footprints:Wirepad, F.Cu at (172.3, 53.4)
- added Din1: Conn_01x01, Footprints:Wirepad, F.Cu at (190.3, 53.4)
- added Din1: Conn_01x01, Footprints:Wirepad, F.Cu at (136.3, 53.4)
- added Din1: Conn_01x01, Footprints:Wirepad, F.Cu at (154.3, 53.4)
- added Din1: Conn_01x01, Footprints:Wirepad, F.Cu at (118.3, 53.4)
- added Din1: Conn_01x01, Footprints:Wirepad, F.Cu at (100.3, 53.4)
- added Din1: Conn_01x01, Footprints:Wirepad, F.Cu at (118.3, 143.4)
- added Din1: Conn_01x01, Footprints:Wirepad, F.Cu at (190.3, 143.4)
- added Din1: Conn_01x01, Footprints:Wirepad, F.Cu at (172.3, 143.4)
- added Din1: Conn_01x01, Footprints:Wirepad, F.Cu at (154.3, 143.4)
- added Din1: Conn_01x01, Footprints:Wirepad, F.Cu at (136.3, 143.4)
- added Din1: Conn_01x01, Footprints:Wirepad, F.Cu at (190.3, 125.4)
- added Dout1: Conn_01x01, Footprints:Wirepad, F.Cu at (85.0, 127.4)
- added Dout1: Conn_01x01, Footprints:Wirepad, F.Cu at (175.0, 127.4)
- added Dout1: Conn_01x01, Footprints:Wirepad, F.Cu at (139.0, 127.4)
- added Dout1: Conn_01x01, Footprints:Wirepad, F.Cu at (121.0, 127.4)
- added Dout1: Conn_01x01, Footprints:Wirepad, F.Cu at (85.0, 91.4)
- added Dout1: Conn_01x01, Footprints:Wirepad, F.Cu at (103.0, 91.4)
- added Dout1: Conn_01x01, Footprints:Wirepad, F.Cu at (85.0, 109.4)
- added Dout1: Conn_01x01, Footprints:Wirepad, F.Cu at (103.0, 109.4)
- added Dout1: Conn_01x01, Footprints:Wirepad, F.Cu at (157.0, 109.4)
- added Dout1: Conn_01x01, Footprints:Wirepad, F.Cu at (175.0, 109.4)
- added Dout1: Conn_01x01, Footprints:Wirepad, F.Cu at (121.0, 109.4)
- added Dout1: Conn_01x01, Footprints:Wirepad, F.Cu at (103.0, 127.4)
- added Dout1: Conn_01x01, Footprints:Wirepad, F.Cu at (139.0, 109.4)
- added Dout1: Conn_01x01, Footprints:Wirepad, F.Cu at (157.0, 91.4)
- added Dout1: Conn_01x01, Footprints:Wirepad, F.Cu at (175.0, 91.4)
- added Dout1: Conn_01x01, Footprints:Wirepad, F.Cu at (139.0, 91.4)
- added Dout1: Conn_01x01, Footprints:Wirepad, F.Cu at (121.0, 91.4)
- added Dout1: Conn_01x01, Footprints:Wirepad, F.Cu at (85.0, 73.4)
- added Dout1: Conn_01x01, Footprints:Wirepad, F.Cu at (103.0, 73.4)
- added Dout1: Conn_01x01, Footprints:Wirepad, F.Cu at (157.0, 73.4)
- added Dout1: Conn_01x01, Footprints:Wirepad, F.Cu at (175.0, 73.4)
- added Dout1: Conn_01x01, Footprints:Wirepad, F.Cu at (139.0, 73.4)
- added Dout1: Conn_01x01, Footprints:Wirepad, F.Cu at (85.0, 145.4)
- added Dout1: Conn_01x01, Footprints:Wirepad, F.Cu at (121.0, 73.4)
- added Dout1: Conn_01x01, Footprints:Wirepad, F.Cu at (157.0, 55.4)
- added Dout1: Conn_01x01, Footprints:Wirepad, F.Cu at (175.0, 55.4)
- added Dout1: Conn_01x01, Footprints:Wirepad, F.Cu at (121.0, 55.4)
- added Dout1: Conn_01x01, Footprints:Wirepad, F.Cu at (139.0, 55.4)
- added Dout1: Conn_01x01, Footprints:Wirepad, F.Cu at (103.0, 55.4)
- added Dout1: Conn_01x01, Footprints:Wirepad, F.Cu at (85.0, 55.4)
- added Dout1: Conn_01x01, Footprints:Wirepad, F.Cu at (103.0, 145.4)
- added Dout1: Conn_01x01, Footprints:Wirepad, F.Cu at (157.0, 145.4)
- added Dout1: Conn_01x01, Footprints:Wirepad, F.Cu at (175.0, 145.4)
- added Dout1: Conn_01x01, Footprints:Wirepad, F.Cu at (121.0, 145.4)
- added Dout1: Conn_01x01, Footprints:Wirepad, F.Cu at (139.0, 145.4)
- added Dout1: Conn_01x01, Footprints:Wirepad, F.Cu at (157.0, 127.4)
- added GND1: Conn_01x01, Footprints:Wirepad, F.Cu at (85.0, 129.2)
- added GND1: Conn_01x01, Footprints:Wirepad, F.Cu at (157.0, 129.2)
- added GND1: Conn_01x01, Footprints:Wirepad, F.Cu at (139.0, 129.2)
- added GND1: Conn_01x01, Footprints:Wirepad, F.Cu at (121.0, 129.2)
- added GND1: Conn_01x01, Footprints:Wirepad, F.Cu at (85.0, 93.2)
- added GND1: Conn_01x01, Footprints:Wirepad, F.Cu at (103.0, 93.2)
- added GND1: Conn_01x01, Footprints:Wirepad, F.Cu at (85.0, 111.2)
- added GND1: Conn_01x01, Footprints:Wirepad, F.Cu at (103.0, 111.2)
- added GND1: Conn_01x01, Footprints:Wirepad, F.Cu at (175.0, 111.2)
- added GND1: Conn_01x01, Footprints:Wirepad, F.Cu at (157.0, 111.2)
- added GND1: Conn_01x01, Footprints:Wirepad, F.Cu at (139.0, 111.2)
- added GND1: Conn_01x01, Footprints:Wirepad, F.Cu at (103.0, 129.2)
- added GND1: Conn_01x01, Footprints:Wirepad, F.Cu at (121.0, 111.2)
- added GND1: Conn_01x01, Footprints:Wirepad, F.Cu at (175.0, 93.2)
- added GND1: Conn_01x01, Footprints:Wirepad, F.Cu at (157.0, 93.2)
- added GND1: Conn_01x01, Footprints:Wirepad, F.Cu at (139.0, 93.2)
- added GND1: Conn_01x01, Footprints:Wirepad, F.Cu at (121.0, 93.2)
- added GND1: Conn_01x01, Footprints:Wirepad, F.Cu at (85.0, 75.2)
- added GND1: Conn_01x01, Footprints:Wirepad, F.Cu at (103.0, 75.2)
- added GND1: Conn_01x01, Footprints:Wirepad, F.Cu at (175.0, 75.2)
- added GND1: Conn_01x01, Footprints:Wirepad, F.Cu at (157.0, 75.2)
- added GND1: Conn_01x01, Footprints:Wirepad, F.Cu at (139.0, 75.2)
- added GND1: Conn_01x01, Footprints:Wirepad, F.Cu at (85.0, 147.2)
- added GND1: Conn_01x01, Footprints:Wirepad, F.Cu at (121.0, 75.2)
- added GND1: Conn_01x01, Footprints:Wirepad, F.Cu at (157.0, 57.2)
- added GND1: Conn_01x01, Footprints:Wirepad, F.Cu at (175.0, 57.2)
- added GND1: Conn_01x01, Footprints:Wirepad, F.Cu at (121.0, 57.2)
- added GND1: Conn_01x01, Footprints:Wirepad, F.Cu at (139.0, 57.2)
- added GND1: Conn_01x01, Footprints:Wirepad, F.Cu at (103.0, 57.2)
- added GND1: Conn_01x01, Footprints:Wirepad, F.Cu at (85.0, 57.2)
- added GND1: Conn_01x01, Footprints:Wirepad, F.Cu at (103.0, 147.2)
- added GND1: Conn_01x01, Footprints:Wirepad, F.Cu at (175.0, 147.2)
- added GND1: Conn_01x01, Footprints:Wirepad, F.Cu at (157.0, 147.2)
- added GND1: Conn_01x01, Footprints:Wirepad, F.Cu at (139.0, 147.2)
- added GND1: Conn_01x01, Footprints:Wirepad, F.Cu at (121.0, 147.2)
- added GND1: Conn_01x01, Footprints:Wirepad, F.Cu at (175.0, 129.2)
- added GND2: Conn_01x01, Footprints:Wirepad, F.Cu at (100.3, 127.2)
- added GND2: Conn_01x01, Footprints:Wirepad, F.Cu at (190.3, 127.2)
- added GND2: Conn_01x01, Footprints:Wirepad, F.Cu at (154.3, 127.2)
- added GND2: Conn_01x01, Footprints:Wirepad, F.Cu at (136.3, 127.2)
- added GND2: Conn_01x01, Footprints:Wirepad, F.Cu at (100.3, 91.2)
- added GND2: Conn_01x01, Footprints:Wirepad, F.Cu at (118.3, 91.2)
- added GND2: Conn_01x01, Footprints:Wirepad, F.Cu at (100.3, 109.2)
- added GND2: Conn_01x01, Footprints:Wirepad, F.Cu at (118.3, 109.2)
- added GND2: Conn_01x01, Footprints:Wirepad, F.Cu at (172.3, 109.2)
- added GND2: Conn_01x01, Footprints:Wirepad, F.Cu at (190.3, 109.2)
- added GND2: Conn_01x01, Footprints:Wirepad, F.Cu at (136.3, 109.2)
- added GND2: Conn_01x01, Footprints:Wirepad, F.Cu at (118.3, 127.2)
- added GND2: Conn_01x01, Footprints:Wirepad, F.Cu at (154.3, 109.2)
- added GND2: Conn_01x01, Footprints:Wirepad, F.Cu at (172.3, 91.2)
- added GND2: Conn_01x01, Footprints:Wirepad, F.Cu at (190.3, 91.2)
- added GND2: Conn_01x01, Footprints:Wirepad, F.Cu at (154.3, 91.2)
- added GND2: Conn_01x01, Footprints:Wirepad, F.Cu at (136.3, 91.2)
- added GND2: Conn_01x01, Footprints:Wirepad, F.Cu at (100.3, 73.2)
- added GND2: Conn_01x01, Footprints:Wirepad, F.Cu at (118.3, 73.2)
- added GND2: Conn_01x01, Footprints:Wirepad, F.Cu at (172.3, 73.2)
- added GND2: Conn_01x01, Footprints:Wirepad, F.Cu at (190.3, 73.2)
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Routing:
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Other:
- board size 106 x 106 mm -> 107 x 107 mm
- net class Default: clearance 0.3 -> 0.1; trace_width 0.8 -> 0.25; via_dia 0.8 -> 0.4; via_drill 0.4 -> 0.3
- rule trace_clearance: 0.3 -> 0.1
- board text added: "-"
- board text added: "Choc"
- board text added: "Din"
- board text added: "Dout"
- board text added: "GND"
- board text added: "HIDTech"
- board text added: "Kompacted"
- board text added: "MX"
- board text added: "Rev 2.0"
- board text added: "VCC"
- board text removed: "ProtoCases.com"
- board text removed: "v1.1"
